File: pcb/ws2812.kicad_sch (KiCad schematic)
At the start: 37 parts

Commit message: Added part numbers for assembly
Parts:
- R9: LCSC (none) -> C25104
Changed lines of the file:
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@@
+      (effects (font (size 1.27 1.27)) hide)
+    )
+    (property "LCSC" "C25104" (id 4) (at 100.33 64.77 0)
       (effects (font (size 1.27 1.27)) hide)
     )

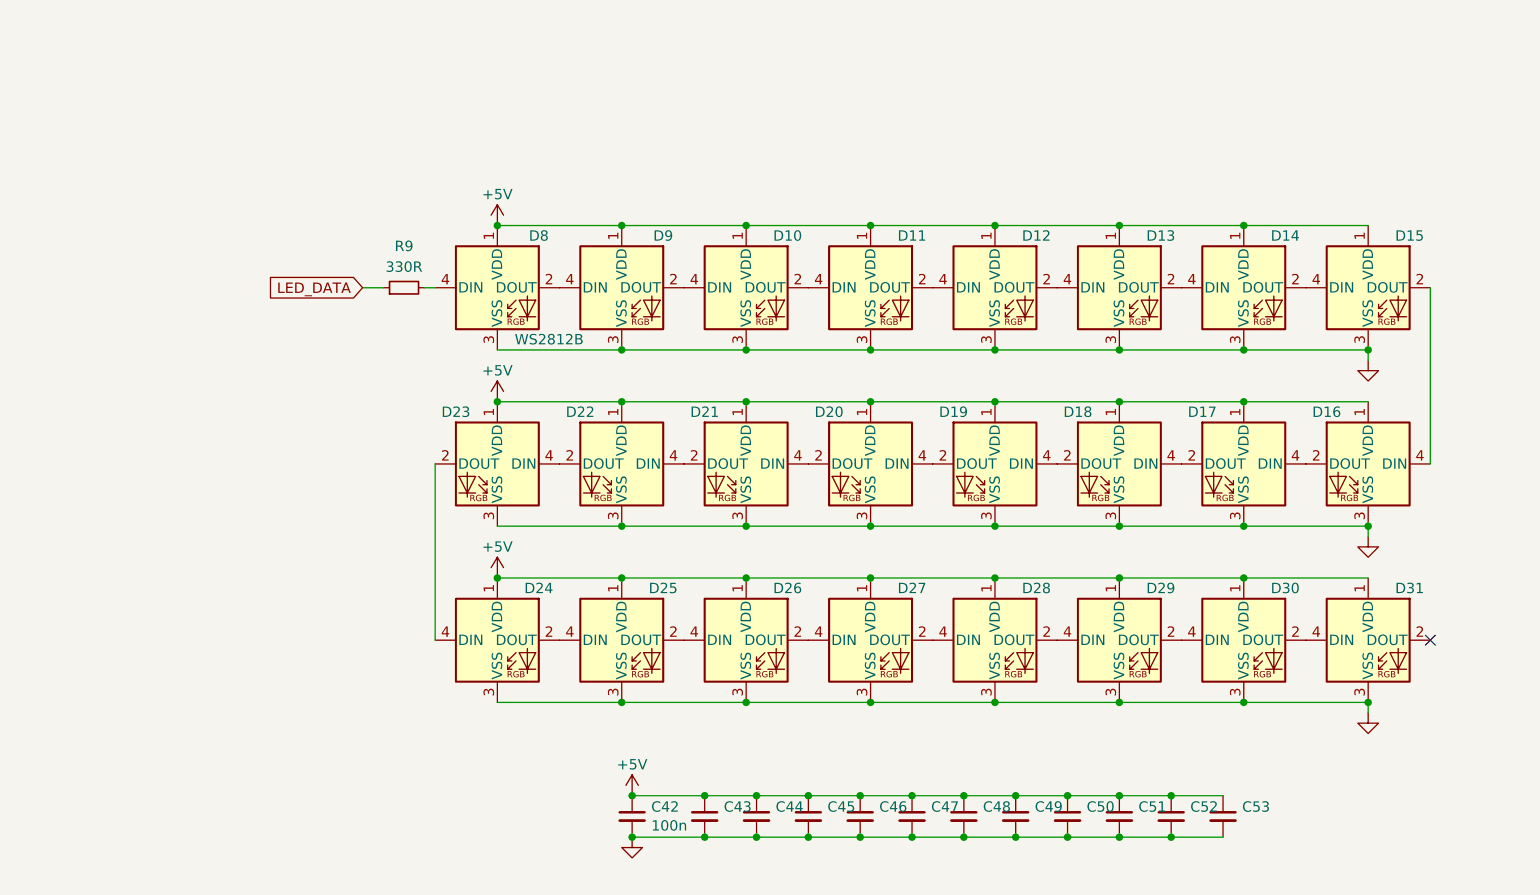
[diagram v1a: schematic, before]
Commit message: Started work on discrete led displays
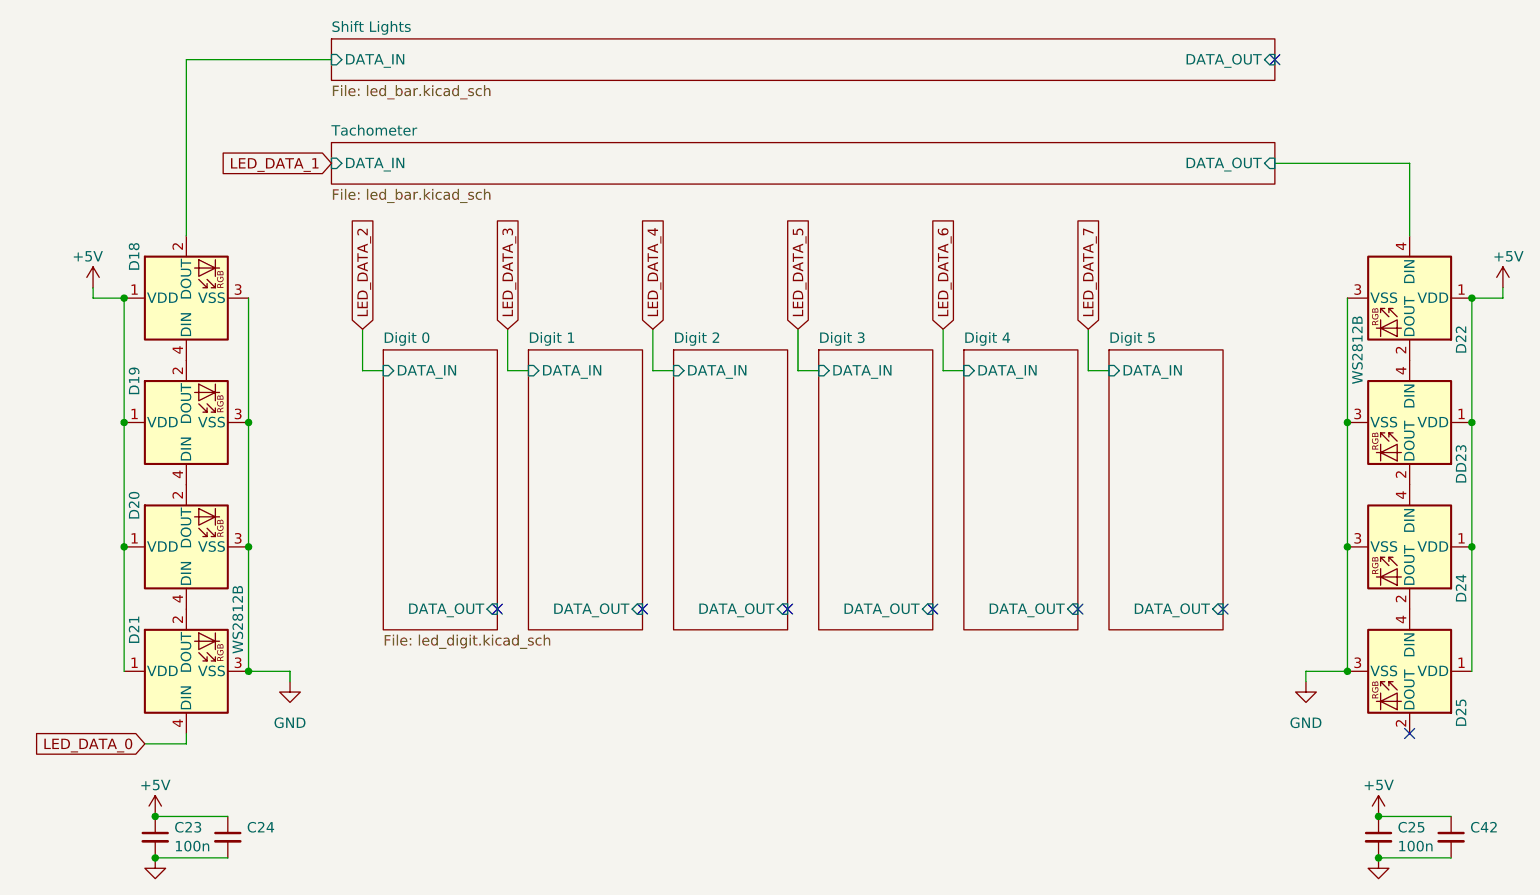
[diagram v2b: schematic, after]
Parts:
- removed C43, C44, C45, C46, C47, C48, C49, C50, C51, C52, C53: 100n, Capacitor_SMD:C_0402_1005Metric, symbol Device:C_Small
- removed D10, D11, D12, D13, D14, D15, D16, D17, D23, D26, D27, D28, D29, D30, D31, D8, D9: WS2812B, LED_SMD:LED_WS2812B_PLCC4_5.0x5.0mm_P3.2mm, symbol LED:WS2812B
- removed R9: 330R, Resistor_SMD:R_0402_1005Metric, symbol Device:R_Small
- added C23, C24, C25: 100n, Capacitor_SMD:C_0402_1005Metric, symbol Device:C_Small
- added DD23: WS2812B, LED_SMD:LED_WS2812B_PLCC4_5.0x5.0mm_P3.2mm, symbol LED:WS2812B
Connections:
- net +5V: now also C23.1, C24.1, C25.1, DD23.1 (VDD)
- net GND: now also C23.2, C24.2, C25.2, DD23.3 (VSS)
- net at D22.2 (DOUT): now also DD23.4 (DIN)
- net at D21.2 (DOUT): now also D20.4 (DIN); no longer D22.4 (DIN)
- net at D19.2 (DOUT): now also D18.4 (DIN); no longer D20.4 (DIN)
- net at D19.4 (DIN): now also D20.2 (DOUT); no longer D18.2 (DOUT)
- net at D24.4 (DIN): now also DD23.2 (DOUT)
- net LED_DATA_0: now reaches D21.4 (DIN)
- net LED_DATA_0: no longer D20.2 (DOUT)
- new net Shift Lights/DATA_IN: D18.2 (DOUT)
- new net Tachometer/DATA_OUT: D22.4 (DIN)
- no-connect marks 1 -> 8
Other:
- added sheet Digit 0 (led_digit.kicad_sch)
- added sheet Digit 1 (led_digit.kicad_sch)
- added sheet Digit 2 (led_digit.kicad_sch)
- added sheet Digit 3 (led_digit.kicad_sch)
- added sheet Digit 4 (led_digit.kicad_sch)
- added sheet Digit 5 (led_digit.kicad_sch)
- added sheet Shift Lights (led_bar.kicad_sch)
- added sheet Tachometer (led_bar.kicad_sch)
